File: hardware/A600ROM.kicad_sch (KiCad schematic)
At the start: 12 parts, among them J2 Conn_01x05, J3 Conn_01x21_Pin, J5 Conn_01x21_Pin, U1 M29F160F

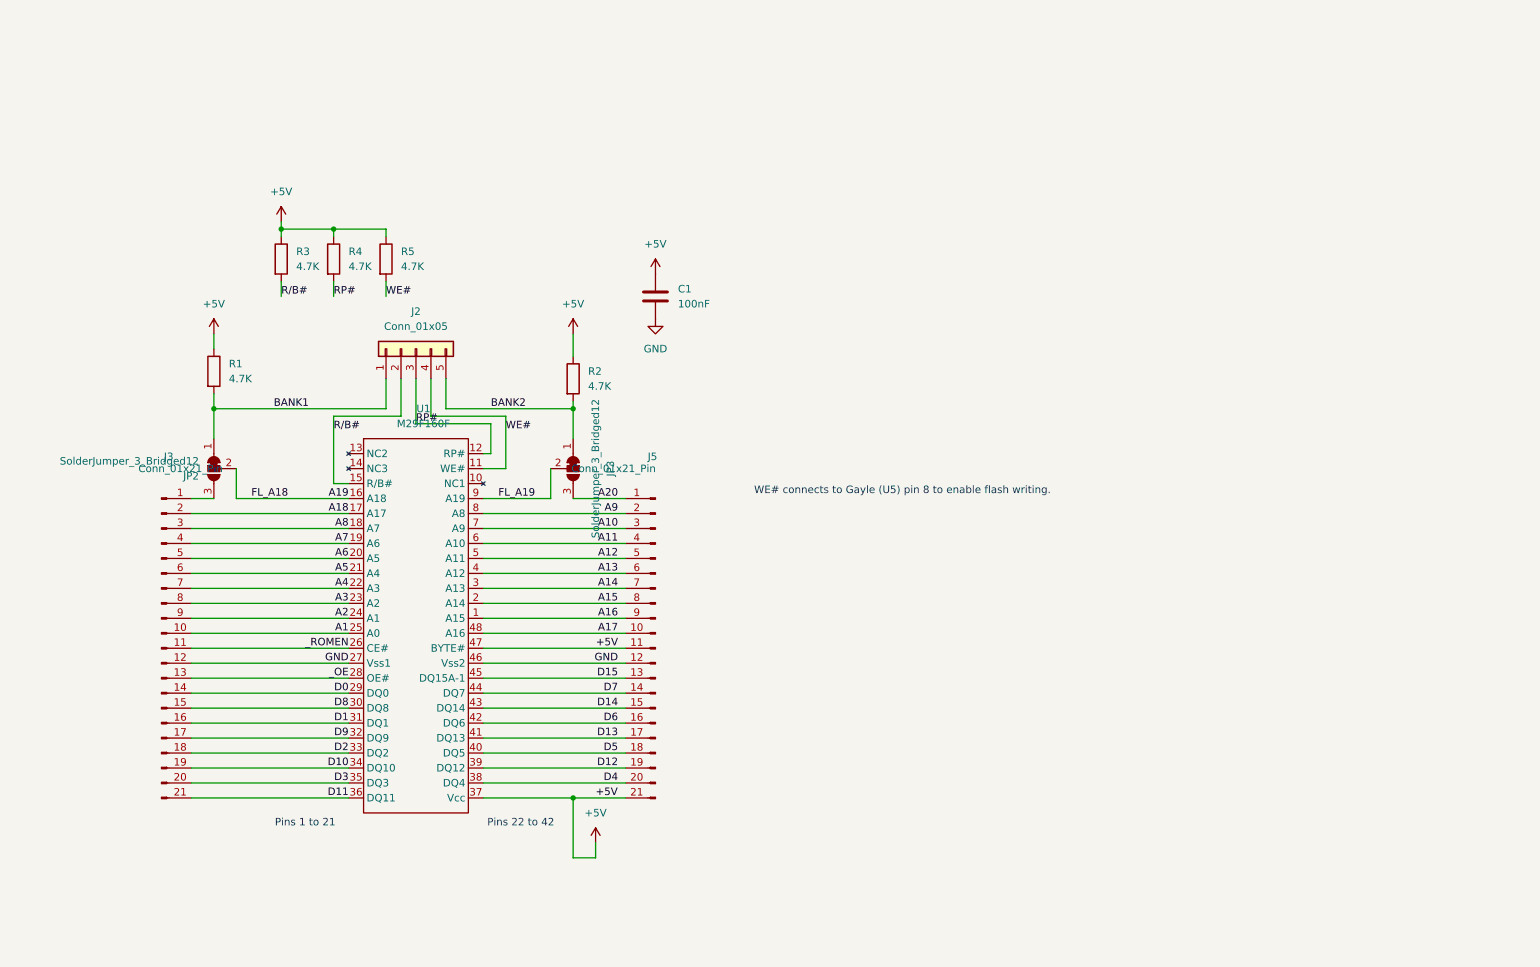
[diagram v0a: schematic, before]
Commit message: Gayle hat
Add hat. Partially unrouted.
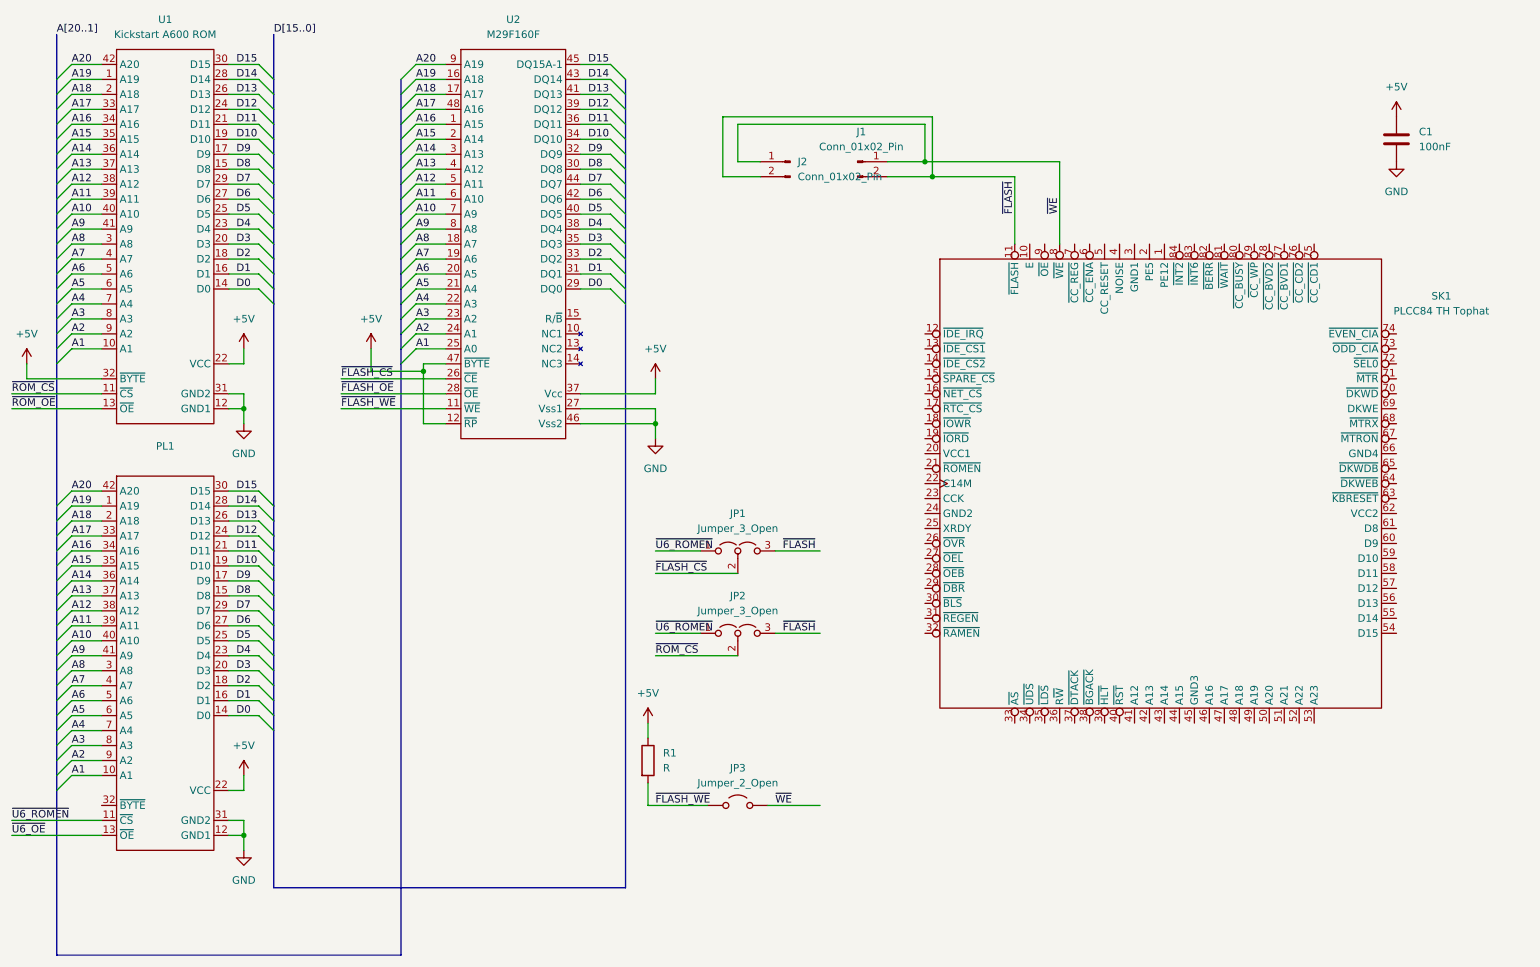
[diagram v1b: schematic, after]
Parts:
- removed J2: Conn_01x05, Connector_PinHeader_2.54mm:PinHeader_1x05_P2.54mm_Vertical, symbol Connector_Generic:Conn_01x05
- removed J3, J5: Conn_01x21_Pin, Connector_PinHeader_2.54mm:PinHeader_1x21_P2.54mm_Vertical, symbol Connector:Conn_01x21_Pin
- removed JP2, JP3: SolderJumper_3_Bridged12, Jumper:SolderJumper-3_P1.3mm_Bridged12_RoundedPad1.0x1.5mm, symbol Jumper:SolderJumper_3_Bridged12
- removed R2, R3, R4, R5: 4.7K, Resistor_SMD:R_0603_1608Metric_Pad0.98x0.95mm_HandSolder, symbol Device:R
- removed U1: M29F160F, Package_SO:TSOP-I-48_18.4x12mm_P0.5mm, symbol Memory_Flash:M29F160F
- added J1, J2: Conn_01x02_Pin, Connector_PinHeader_2.54mm:PinHeader_1x02_P2.54mm_Vertical, symbol Connector:Conn_01x02_Pin
- added JP1, JP2: Jumper_3_Open, Connector_PinHeader_2.54mm:PinHeader_1x03_P2.54mm_Vertical, symbol Jumper:Jumper_3_Open
- added JP3: Jumper_2_Open, Connector_PinHeader_2.54mm:PinHeader_1x02_P2.54mm_Vertical, symbol Jumper:Jumper_2_Open
- added PL1: ~, Package_DIP:DIP-42_W15.24mm, symbol A600ROM:Kickstart_Header
- added SK1: PLCC84 TH Tophat, A600ROM:PLCC-84_THT-Socket-Tophat, symbol A600ROM:Gayle_Tophat
- added U1: Kickstart A600 ROM, Package_DIP:DIP-42_W15.24mm, symbol A600ROM:Kickstart_ROM
- added U2: M29F160F, Package_SO:TSOP-I-48_18.4x12mm_P0.5mm, symbol A600ROM:M29F160F
- R1: value 4.7K -> R; footprint Resistor_SMD:R_0603_1608Metric_Pad0.98x0.95mm_HandSolder -> Resistor_SMD:R_0805_2012Metric_Pad1.20x1.40mm_HandSolder
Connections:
- net +5V: now also PL1.22 (VCC), U1.22 (VCC), U1.32 (~{BYTE}), U2.12 (~{RP}), U2.37 (Vcc), U2.47 (~{BYTE})
- net A1: now also PL1.10 (A1), U1.10 (A1), U2.25 (A0)
- net A10: now also PL1.40 (A10), U1.40 (A10), U2.7 (A9)
- net A11: now also PL1.39 (A11), U1.39 (A11), U2.6 (A10)
- net A12: now also PL1.38 (A12), U1.38 (A12), U2.5 (A11)
- net A13: now also PL1.37 (A13), U1.37 (A13), U2.4 (A12)
- net A14: now also PL1.36 (A14), U1.36 (A14), U2.3 (A13)
- net A15: now also PL1.35 (A15), U1.35 (A15), U2.2 (A14)
- net A16: now also PL1.34 (A16), U1.34 (A16), U2.1 (A15)
- net A17: now also PL1.33 (A17), U1.33 (A17), U2.48 (A16)
- net A18: now also PL1.2 (A18), U1.2 (A18), U2.17 (A17)
- net A19: now also PL1.1 (A19), U1.1 (A19), U2.16 (A18)
- net A2: now also PL1.9 (A2), U1.9 (A2), U2.24 (A1)
- net A20: now also PL1.42 (A20), U1.42 (A20), U2.9 (A19)
- net A3: now also PL1.8 (A3), U1.8 (A3), U2.23 (A2)
- net A4: now also PL1.7 (A4), U1.7 (A4), U2.22 (A3)
- net A5: now also PL1.6 (A5), U1.6 (A5), U2.21 (A4)
- net A6: now also PL1.5 (A6), U1.5 (A6), U2.20 (A5)
- net A7: now also PL1.4 (A7), U1.4 (A7), U2.19 (A6)
- net A8: now also PL1.3 (A8), U1.3 (A8), U2.18 (A7)
- net A9: now also PL1.41 (A9), U1.41 (A9), U2.8 (A8)
- net D0: now also PL1.14 (D0), U1.14 (D0), U2.29 (DQ0)
- net D1: now also PL1.16 (D1), U1.16 (D1), U2.31 (DQ1)
- net D10: now also PL1.19 (D10), U1.19 (D10), U2.34 (DQ10)
- net D11: now also PL1.21 (D11), U1.21 (D11), U2.36 (DQ11)
- net D12: now also PL1.24 (D12), U1.24 (D12), U2.39 (DQ12)
- net D13: now also PL1.26 (D13), U1.26 (D13), U2.41 (DQ13)
- net D14: now also PL1.28 (D14), U1.28 (D14), U2.43 (DQ14)
- net D15: now also PL1.30 (D15), U1.30 (D15), U2.45 (DQ15A-1)
- net D2: now also PL1.18 (D2), U1.18 (D2), U2.33 (DQ2)
- net D3: now also PL1.20 (D3), U1.20 (D3), U2.35 (DQ3)
- net D4: now also PL1.23 (D4), U1.23 (D4), U2.38 (DQ4)
- net D5: now also PL1.25 (D5), U1.25 (D5), U2.40 (DQ5)
- net D6: now also PL1.27 (D6), U1.27 (D6), U2.42 (DQ6)
- net D7: now also PL1.29 (D7), U1.29 (D7), U2.44 (DQ7)
- net D8: now also PL1.15 (D8), U1.15 (D8), U2.30 (DQ8)
- net D9: now also PL1.17 (D9), U1.17 (D9), U2.32 (DQ9)
- net GND: now also PL1.12 (GND1), PL1.31 (GND2), U1.12 (GND1), U1.31 (GND2), U2.27 (Vss1), U2.46 (Vss2)
- net BANK1 renamed ~{FLASH_WE}
- net ~{FLASH_WE}: now also JP3.1 (A), U2.11 (~{WE})
- new net ~{FLASH_CS}: JP1.2 (C), U2.26 (~{CE})
- new net ~{FLASH_OE}: U2.28 (~{OE})
- new net ~{FLASH}: J1.2 (Pin_2), J2.2 (Pin_2), JP1.3 (B), JP2.3 (B), SK1.11 (~{FLASH})
- new net ~{ROM_CS}: JP2.2 (C), U1.11 (~{CS})
- new net ~{ROM_OE}: U1.13 (~{OE})
- new net ~{U6_OE}: PL1.13 (~{OE})
- new net ~{U6_ROMEN}: JP1.1 (A), JP2.1 (A), PL1.11 (~{CS})
- new net ~{WE}: J1.1 (Pin_1), J2.1 (Pin_1), JP3.2 (B), SK1.8 (~{WE})
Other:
- note removed: "Pins 1 to 21"
- note removed: "Pins 22 to 42"
- note removed: "WE# connects to Gayle (U5) pin 8 to enable flash writing."
- moved on the sheet: C1

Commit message: Add connectors
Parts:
- added U3: 74HC86, symbol 74xx:74HC86
- PL1: footprint Package_DIP:DIP-42_W15.24mm -> A600ROM:DIP-42_W15.24mm_SMDHeader_SmallPads
- U1: footprint Package_DIP:DIP-42_W15.24mm -> A600ROM:DIP-42_W15.24mm_SMDSocket_SmallPads
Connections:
- net A19: no longer U2.16 (A18)
- net A20: no longer U2.9 (A19)
- net ~{FLASH}: no longer J1.2 (Pin_2), J2.2 (Pin_2), JP1.3 (B), SK1.11 (~{FLASH})
- net ~{U6_ROMEN} renamed ~{U6_CS}
- new net ~{FLASH}_GAYLE: J1.2 (Pin_2), J2.2 (Pin_2), SK1.11 (~{FLASH})
- new net ~{U5_FLASH}: JP1.3 (B)
